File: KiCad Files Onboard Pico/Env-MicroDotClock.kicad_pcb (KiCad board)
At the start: 2 copper layers, 110 x 80 mm, 95 parts, among them IC1 IS31FL3730-QFLS2-TR, IC2 IS31FL3730-QFLS2-TR, IC3 IS31FL3730-QFLS2-TR, IC4 IS31FL3730-QFLS2-TR, J1 1mm 1x3, J2 GT-USB-7051A, J3 Button, J4 TYPE-C-31-M-12, M1 Dip-14 Socket, M2 Dip-14 Socket, M3 Dip-14 Socket, M4 Dip-14 Socket, M5 Dip-14 Socket, M6 Dip-14 Socket, M7 Dip-14 Socket, M8 Dip-14 Socket, Q1 2SC1815, SW1 MX Keyboard Switch, SW2 MX Keyboard Switch, SW3 MX Keyboard Switch, SW4 MX Keyboard Switch, SW5 MX Keyboard Switch, U1 TCA9406DC, U2 TPS63001DRCR, U3 DS3231M, U4 RP2040, Y1 3225_4P 12MHz

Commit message: removed sockets, added level shifter IC, changed RTC to smaller package, re-did entire board to be more tidy.
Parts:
- removed C23: 1uf 0402, Capacitor_SMD:C_0402_1005Metric
- removed C24, C26, C27, C28, C29, C30, C31: 100nf 0402, Capacitor_SMD:C_0402_1005Metric
- removed C25: 2.2uF 0402, Capacitor_SMD:C_0402_1005Metric
- removed C32: 10uF 0402, Capacitor_SMD:C_0402_1005Metric
- removed FLASH1: W25Q16JVUXIQ, Package_SON:SON-8-1EP_3x2mm_P0.5mm_EP1.4x1.6mm
- removed J2: GT-USB-7051A, Connector_USB:USB_C_Receptacle_G-Switch_GT-USB-7051x
- removed J3: Button, Button_Switch_SMD:SW_Push_SPST_NO_Alps_SKRK
- removed J4: TYPE-C-31-M-12, Connector_USB:USB_C_Receptacle_HRO_TYPE-C-31-M-12
- removed L1: SPH3015H2R2MT, Inductor_SMD:L_Sunlord_SWPA3015S
- removed M1, M2, M3, M4, M5, M6, M7, M8: Dip-14 Socket, Package_DIP:DIP-14_W7.62mm_Socket
- removed R14, R17: 5.1K 0805, Resistor_SMD:R_0805_2012Metric
- removed R15, R16: 5.1K 0402, Resistor_SMD:R_0402_1005Metric
- removed R18, R23: 1K 0402, Resistor_SMD:R_0402_1005Metric
- removed R19: 100ohm 0402, Resistor_SMD:R_0402_1005Metric
- removed R21: 10K 0402, Resistor_SMD:R_0402_1005Metric
- removed R24, R25: 27r 0402 resistor, Resistor_SMD:R_0402_1005Metric
- removed RSW1: TSA343G00-250J2, Button_Switch_SMD:SW_Push_SPST_NO_Alps_SKRK
- removed TP1, TP2, TP3: TestPoint, TestPoint:TestPoint_Pad_D1.0mm
- removed U2: TPS63001DRCR, Package_SON:Texas_DRC0010J_ThermalVias
- removed U4: RP2040, MCU_RaspberryPi_and_Boards:RP2040-QFN-56
- removed Y1: 3225_4P 12MHz, Crystal:Crystal_SMD_3225-4Pin_3.2x2.5mm
- added C201: 10uF 0402, Capacitor_SMD:C_0402_1005Metric, F.Cu at (81.7, 62.6)
- added C202: 0.1uF 0402, Capacitor_SMD:C_0402_1005Metric, F.Cu at (86.9, 60.6)
- added C203: 22pf 0402, Capacitor_SMD:C_0402_1005Metric, F.Cu at (62.5, 69.9)
- added C204: 22pf 0402, Capacitor_SMD:C_0402_1005Metric, F.Cu at (67.3, 72.5)
- added C205: 100nf 0402, Capacitor_SMD:C_0402_1005Metric, F.Cu at (66.2, 54.9)
- added C206: 10uF 0402, Capacitor_SMD:C_0402_1005Metric, F.Cu at (74.1, 56.2)
- added C207: 10uF 0402, Capacitor_SMD:C_0402_1005Metric, F.Cu at (75.0, 56.2)
- added C208: 100nf 0402, Capacitor_SMD:C_0402_1005Metric, F.Cu at (69.7, 69.5)
- added C209: 100nf 0402, Capacitor_SMD:C_0402_1005Metric, F.Cu at (67.5, 55.9)
- added C210: 1uf 0402, Capacitor_SMD:C_0402_1005Metric, F.Cu at (71.5, 55.9)
- added C211: 100nf 0402, Capacitor_SMD:C_0402_1005Metric, F.Cu at (73.6, 60.0)
- added C212: 2.2uF 0402, Capacitor_SMD:C_0402_1005Metric, F.Cu at (72.5, 55.9)
- added C213: 100nf 0402, Capacitor_SMD:C_0402_1005Metric, F.Cu at (74.6, 64.0)
- added C214: 100nf 0402, Capacitor_SMD:C_0402_1005Metric, F.Cu at (68.7, 69.5)
- added C215: 100nf 0402, Capacitor_SMD:C_0402_1005Metric, F.Cu at (62.3, 64.0)
- added C216: 100nf 0402, Capacitor_SMD:C_0402_1005Metric, F.Cu at (62.9, 59.7)
- added C217: 100nf 0402, Capacitor_SMD:C_0402_1005Metric, F.Cu at (68.5, 55.9)
- added C218: 100nf 0402, Capacitor_SMD:C_0402_1005Metric, F.Cu at (73.6, 59.0)
- added D10: LED 0402 10mA, LED_SMD:LED_0402_1005Metric, F.Cu at (35.5, 29.8)
- added D100: LED 0402 10mA, LED_SMD:LED_0402_1005Metric, F.Cu at (56.5, 37.8)
- added D101: LED 0402 10mA, LED_SMD:LED_0402_1005Metric, F.Cu at (56.5, 39.8)
- added D102: LED 0402 10mA, LED_SMD:LED_0402_1005Metric, F.Cu at (58.0, 27.8)
- added D103: LED 0402 10mA, LED_SMD:LED_0402_1005Metric, F.Cu at (58.0, 29.8)
- added D104: LED 0402 10mA, LED_SMD:LED_0402_1005Metric, F.Cu at (58.0, 31.8)
- added D105: LED 0402 10mA, LED_SMD:LED_0402_1005Metric, F.Cu at (58.0, 33.8)
- added D106: LED 0402 10mA, LED_SMD:LED_0402_1005Metric, F.Cu at (58.0, 35.8)
- added D107: LED 0402 10mA, LED_SMD:LED_0402_1005Metric, F.Cu at (58.0, 37.8)
- added D108: LED 0402 10mA, LED_SMD:LED_0402_1005Metric, F.Cu at (58.0, 39.8)
- added D109: LED 0402 10mA, LED_SMD:LED_0402_1005Metric, F.Cu at (59.5, 39.8)
- added D11: LED 0402 10mA, LED_SMD:LED_0402_1005Metric, F.Cu at (35.5, 31.8)
- added D110: LED 0402 10mA, LED_SMD:LED_0402_1005Metric, F.Cu at (61.0, 27.8)
- added D111: LED 0402 10mA, LED_SMD:LED_0402_1005Metric, F.Cu at (61.0, 29.8)
- added D112: LED 0402 10mA, LED_SMD:LED_0402_1005Metric, F.Cu at (61.0, 31.8)
- added D113: LED 0402 10mA, LED_SMD:LED_0402_1005Metric, F.Cu at (61.0, 33.8)
- added D114: LED 0402 10mA, LED_SMD:LED_0402_1005Metric, F.Cu at (61.0, 35.8)
- added D115: LED 0402 10mA, LED_SMD:LED_0402_1005Metric, F.Cu at (61.0, 37.8)
- added D116: LED 0402 10mA, LED_SMD:LED_0402_1005Metric, F.Cu at (61.0, 39.8)
- added D117: LED 0402 10mA, LED_SMD:LED_0402_1005Metric, F.Cu at (62.5, 27.8)
- added D118: LED 0402 10mA, LED_SMD:LED_0402_1005Metric, F.Cu at (62.5, 29.8)
- added D119: LED 0402 10mA, LED_SMD:LED_0402_1005Metric, F.Cu at (62.5, 31.8)
- added D12: LED 0402 10mA, LED_SMD:LED_0402_1005Metric, F.Cu at (35.5, 33.8)
- added D120: LED 0402 10mA, LED_SMD:LED_0402_1005Metric, F.Cu at (62.5, 33.8)
- added D121: LED 0402 10mA, LED_SMD:LED_0402_1005Metric, F.Cu at (62.5, 35.8)
- added D122: LED 0402 10mA, LED_SMD:LED_0402_1005Metric, F.Cu at (62.5, 37.8)
- added D123: LED 0402 10mA, LED_SMD:LED_0402_1005Metric, F.Cu at (62.5, 39.8)
- added D124: LED 0402 10mA, LED_SMD:LED_0402_1005Metric, F.Cu at (64.0, 27.8)
- added D125: LED 0402 10mA, LED_SMD:LED_0402_1005Metric, F.Cu at (64.0, 29.8)
- added D126: LED 0402 10mA, LED_SMD:LED_0402_1005Metric, F.Cu at (64.0, 31.8)
- added D127: LED 0402 10mA, LED_SMD:LED_0402_1005Metric, F.Cu at (64.0, 33.8)
- added D128: LED 0402 10mA, LED_SMD:LED_0402_1005Metric, F.Cu at (64.0, 35.8)
- added D129: LED 0402 10mA, LED_SMD:LED_0402_1005Metric, F.Cu at (64.0, 37.8)
- added D13: LED 0402 10mA, LED_SMD:LED_0402_1005Metric, F.Cu at (35.5, 35.8)
- added D130: LED 0402 10mA, LED_SMD:LED_0402_1005Metric, F.Cu at (64.0, 39.8)
- added D131: LED 0402 10mA, LED_SMD:LED_0402_1005Metric, F.Cu at (65.5, 27.8)
- added D132: LED 0402 10mA, LED_SMD:LED_0402_1005Metric, F.Cu at (65.5, 29.8)
- added D133: LED 0402 10mA, LED_SMD:LED_0402_1005Metric, F.Cu at (65.5, 31.8)
- added D134: LED 0402 10mA, LED_SMD:LED_0402_1005Metric, F.Cu at (65.5, 33.8)
- added D135: LED 0402 10mA, LED_SMD:LED_0402_1005Metric, F.Cu at (65.5, 35.8)
- added D136: LED 0402 10mA, LED_SMD:LED_0402_1005Metric, F.Cu at (65.5, 37.8)
- added D137: LED 0402 10mA, LED_SMD:LED_0402_1005Metric, F.Cu at (65.5, 39.8)
- added D138: LED 0402 10mA, LED_SMD:LED_0402_1005Metric, F.Cu at (67.0, 27.8)
- added D139: LED 0402 10mA, LED_SMD:LED_0402_1005Metric, F.Cu at (67.0, 29.8)
- added D14: LED 0402 10mA, LED_SMD:LED_0402_1005Metric, F.Cu at (35.5, 37.8)
- added D140: LED 0402 10mA, LED_SMD:LED_0402_1005Metric, F.Cu at (67.0, 31.8)
- added D141: LED 0402 10mA, LED_SMD:LED_0402_1005Metric, F.Cu at (67.0, 33.8)
- added D142: LED 0402 10mA, LED_SMD:LED_0402_1005Metric, F.Cu at (67.0, 35.8)
- added D143: LED 0402 10mA, LED_SMD:LED_0402_1005Metric, F.Cu at (67.0, 37.8)
- added D144: LED 0402 10mA, LED_SMD:LED_0402_1005Metric, F.Cu at (67.0, 39.8)
- added D145: LED 0402 10mA, LED_SMD:LED_0402_1005Metric, F.Cu at (68.5, 39.8)
- added D146: LED 0402 10mA, LED_SMD:LED_0402_1005Metric, F.Cu at (70.0, 27.8)
- added D147: LED 0402 10mA, LED_SMD:LED_0402_1005Metric, F.Cu at (70.0, 29.8)
- added D148: LED 0402 10mA, LED_SMD:LED_0402_1005Metric, F.Cu at (70.0, 31.8)
- added D149: LED 0402 10mA, LED_SMD:LED_0402_1005Metric, F.Cu at (70.0, 33.8)
- added D15: LED 0402 10mA, LED_SMD:LED_0402_1005Metric, F.Cu at (35.5, 39.8)
- added D150: LED 0402 10mA, LED_SMD:LED_0402_1005Metric, F.Cu at (70.0, 35.8)
- added D151: LED 0402 10mA, LED_SMD:LED_0402_1005Metric, F.Cu at (70.0, 37.8)
- added D152: LED 0402 10mA, LED_SMD:LED_0402_1005Metric, F.Cu at (70.0, 39.8)
- added D153: LED 0402 10mA, LED_SMD:LED_0402_1005Metric, F.Cu at (71.5, 27.8)
- added D154: LED 0402 10mA, LED_SMD:LED_0402_1005Metric, F.Cu at (71.5, 29.8)
- added D155: LED 0402 10mA, LED_SMD:LED_0402_1005Metric, F.Cu at (71.5, 31.8)
- added D156: LED 0402 10mA, LED_SMD:LED_0402_1005Metric, F.Cu at (71.5, 33.8)
- added D157: LED 0402 10mA, LED_SMD:LED_0402_1005Metric, F.Cu at (71.5, 35.8)
- added D158: LED 0402 10mA, LED_SMD:LED_0402_1005Metric, F.Cu at (71.5, 37.8)
- added D159: LED 0402 10mA, LED_SMD:LED_0402_1005Metric, F.Cu at (71.5, 39.8)
- added D16: LED 0402 10mA, LED_SMD:LED_0402_1005Metric, F.Cu at (37.0, 27.8)
- added D160: LED 0402 10mA, LED_SMD:LED_0402_1005Metric, F.Cu at (73.0, 27.8)
- added D161: LED 0402 10mA, LED_SMD:LED_0402_1005Metric, F.Cu at (73.0, 29.8)
- added D162: LED 0402 10mA, LED_SMD:LED_0402_1005Metric, F.Cu at (73.0, 31.8)
- added D163: LED 0402 10mA, LED_SMD:LED_0402_1005Metric, F.Cu at (73.0, 33.8)
- added D164: LED 0402 10mA, LED_SMD:LED_0402_1005Metric, F.Cu at (73.0, 35.8)
- added D165: LED 0402 10mA, LED_SMD:LED_0402_1005Metric, F.Cu at (73.0, 37.8)
- added D166: LED 0402 10mA, LED_SMD:LED_0402_1005Metric, F.Cu at (73.0, 39.8)
- added D167: LED 0402 10mA, LED_SMD:LED_0402_1005Metric, F.Cu at (74.5, 27.8)
- added D168: LED 0402 10mA, LED_SMD:LED_0402_1005Metric, F.Cu at (74.5, 29.8)
- added D169: LED 0402 10mA, LED_SMD:LED_0402_1005Metric, F.Cu at (74.5, 31.8)
- added D17: LED 0402 10mA, LED_SMD:LED_0402_1005Metric, F.Cu at (37.0, 29.8)
- added D170: LED 0402 10mA, LED_SMD:LED_0402_1005Metric, F.Cu at (74.5, 33.8)
- added D171: LED 0402 10mA, LED_SMD:LED_0402_1005Metric, F.Cu at (74.5, 35.8)
- added D172: LED 0402 10mA, LED_SMD:LED_0402_1005Metric, F.Cu at (74.5, 37.8)
- added D173: LED 0402 10mA, LED_SMD:LED_0402_1005Metric, F.Cu at (74.5, 39.8)
- added D174: LED 0402 10mA, LED_SMD:LED_0402_1005Metric, F.Cu at (76.0, 27.8)
- added D175: LED 0402 10mA, LED_SMD:LED_0402_1005Metric, F.Cu at (76.0, 29.8)
- added D176: LED 0402 10mA, LED_SMD:LED_0402_1005Metric, F.Cu at (76.0, 31.8)
- added D177: LED 0402 10mA, LED_SMD:LED_0402_1005Metric, F.Cu at (76.0, 33.8)
- added D178: LED 0402 10mA, LED_SMD:LED_0402_1005Metric, F.Cu at (76.0, 35.8)
- added D179: LED 0402 10mA, LED_SMD:LED_0402_1005Metric, F.Cu at (76.0, 37.8)
- added D18: LED 0402 10mA, LED_SMD:LED_0402_1005Metric, F.Cu at (37.0, 31.8)
- added D180: LED 0402 10mA, LED_SMD:LED_0402_1005Metric, F.Cu at (76.0, 39.8)
- added D181: LED 0402 10mA, LED_SMD:LED_0402_1005Metric, F.Cu at (77.5, 39.8)
- added D182: LED 0402 10mA, LED_SMD:LED_0402_1005Metric, F.Cu at (79.0, 27.8)
- added D183: LED 0402 10mA, LED_SMD:LED_0402_1005Metric, F.Cu at (79.0, 29.8)
- added D184: LED 0402 10mA, LED_SMD:LED_0402_1005Metric, F.Cu at (79.0, 31.8)
- added D185: LED 0402 10mA, LED_SMD:LED_0402_1005Metric, F.Cu at (79.0, 33.8)
- added D186: LED 0402 10mA, LED_SMD:LED_0402_1005Metric, F.Cu at (79.0, 35.8)
- added D187: LED 0402 10mA, LED_SMD:LED_0402_1005Metric, F.Cu at (79.0, 37.8)
- added D188: LED 0402 10mA, LED_SMD:LED_0402_1005Metric, F.Cu at (79.0, 39.8)
- added D189: LED 0402 10mA, LED_SMD:LED_0402_1005Metric, F.Cu at (80.5, 27.8)
- added D19: LED 0402 10mA, LED_SMD:LED_0402_1005Metric, F.Cu at (37.0, 33.8)
- added D190: LED 0402 10mA, LED_SMD:LED_0402_1005Metric, F.Cu at (80.5, 29.8)
- added D191: LED 0402 10mA, LED_SMD:LED_0402_1005Metric, F.Cu at (80.5, 31.8)
- added D192: LED 0402 10mA, LED_SMD:LED_0402_1005Metric, F.Cu at (80.5, 33.8)
- added D193: LED 0402 10mA, LED_SMD:LED_0402_1005Metric, F.Cu at (80.5, 35.8)
- added D194: LED 0402 10mA, LED_SMD:LED_0402_1005Metric, F.Cu at (80.5, 37.8)
- added D195: LED 0402 10mA, LED_SMD:LED_0402_1005Metric, F.Cu at (80.5, 39.8)
- added D196: LED 0402 10mA, LED_SMD:LED_0402_1005Metric, F.Cu at (82.0, 27.8)
- added D197: LED 0402 10mA, LED_SMD:LED_0402_1005Metric, F.Cu at (82.0, 29.8)
- added D198: LED 0402 10mA, LED_SMD:LED_0402_1005Metric, F.Cu at (82.0, 31.8)
- added D199: LED 0402 10mA, LED_SMD:LED_0402_1005Metric, F.Cu at (82.0, 33.8)
- added D20: LED 0402 10mA, LED_SMD:LED_0402_1005Metric, F.Cu at (37.0, 35.8)
- added D200: LED 0402 10mA, LED_SMD:LED_0402_1005Metric, F.Cu at (82.0, 35.8)
- added D201: LED 0402 10mA, LED_SMD:LED_0402_1005Metric, F.Cu at (82.0, 37.8)
- added D202: LED 0402 10mA, LED_SMD:LED_0402_1005Metric, F.Cu at (82.0, 39.8)
- added D203: LED 0402 10mA, LED_SMD:LED_0402_1005Metric, F.Cu at (83.5, 27.8)
- added D204: LED 0402 10mA, LED_SMD:LED_0402_1005Metric, F.Cu at (83.5, 29.8)
- added D205: LED 0402 10mA, LED_SMD:LED_0402_1005Metric, F.Cu at (83.5, 31.8)
- added D206: LED 0402 10mA, LED_SMD:LED_0402_1005Metric, F.Cu at (83.5, 33.8)
- added D207: LED 0402 10mA, LED_SMD:LED_0402_1005Metric, F.Cu at (83.5, 35.8)
- added D208: LED 0402 10mA, LED_SMD:LED_0402_1005Metric, F.Cu at (83.5, 37.8)
- added D209: LED 0402 10mA, LED_SMD:LED_0402_1005Metric, F.Cu at (83.5, 39.8)
- added D21: LED 0402 10mA, LED_SMD:LED_0402_1005Metric, F.Cu at (37.0, 37.8)
- added D210: LED 0402 10mA, LED_SMD:LED_0402_1005Metric, F.Cu at (85.0, 27.8)
- added D211: LED 0402 10mA, LED_SMD:LED_0402_1005Metric, F.Cu at (85.0, 29.8)
- added D212: LED 0402 10mA, LED_SMD:LED_0402_1005Metric, F.Cu at (85.0, 31.8)
- added D213: LED 0402 10mA, LED_SMD:LED_0402_1005Metric, F.Cu at (85.0, 33.8)
- added D214: LED 0402 10mA, LED_SMD:LED_0402_1005Metric, F.Cu at (85.0, 35.8)
- added D215: LED 0402 10mA, LED_SMD:LED_0402_1005Metric, F.Cu at (85.0, 37.8)
- added D216: LED 0402 10mA, LED_SMD:LED_0402_1005Metric, F.Cu at (85.0, 39.8)
- added D217: LED 0402 10mA, LED_SMD:LED_0402_1005Metric, F.Cu at (86.5, 39.8)
- added D218: LED 0402 10mA, LED_SMD:LED_0402_1005Metric, F.Cu at (88.0, 27.8)
- added D219: LED 0402 10mA, LED_SMD:LED_0402_1005Metric, F.Cu at (88.0, 29.8)
- added D22: LED 0402 10mA, LED_SMD:LED_0402_1005Metric, F.Cu at (37.0, 39.8)
- added D220: LED 0402 10mA, LED_SMD:LED_0402_1005Metric, F.Cu at (88.0, 31.8)
- added D221: LED 0402 10mA, LED_SMD:LED_0402_1005Metric, F.Cu at (88.0, 33.8)
- added D222: LED 0402 10mA, LED_SMD:LED_0402_1005Metric, F.Cu at (88.0, 35.8)
- added D223: LED 0402 10mA, LED_SMD:LED_0402_1005Metric, F.Cu at (88.0, 37.8)
- added D224: LED 0402 10mA, LED_SMD:LED_0402_1005Metric, F.Cu at (88.0, 39.8)
- added D225: LED 0402 10mA, LED_SMD:LED_0402_1005Metric, F.Cu at (89.5, 27.8)
- added D226: LED 0402 10mA, LED_SMD:LED_0402_1005Metric, F.Cu at (89.5, 29.8)
- added D227: LED 0402 10mA, LED_SMD:LED_0402_1005Metric, F.Cu at (89.5, 31.8)
- added D228: LED 0402 10mA, LED_SMD:LED_0402_1005Metric, F.Cu at (89.5, 33.8)
- added D229: LED 0402 10mA, LED_SMD:LED_0402_1005Metric, F.Cu at (89.5, 35.8)
- added D23: LED 0402 10mA, LED_SMD:LED_0402_1005Metric, F.Cu at (38.5, 27.8)
- added D230: LED 0402 10mA, LED_SMD:LED_0402_1005Metric, F.Cu at (89.5, 37.8)
- added D231: LED 0402 10mA, LED_SMD:LED_0402_1005Metric, F.Cu at (89.5, 39.8)
- added D232: LED 0402 10mA, LED_SMD:LED_0402_1005Metric, F.Cu at (91.0, 27.8)
- added D233: LED 0402 10mA, LED_SMD:LED_0402_1005Metric, F.Cu at (91.0, 29.8)
- added D234: LED 0402 10mA, LED_SMD:LED_0402_1005Metric, F.Cu at (91.0, 31.8)
- added D235: LED 0402 10mA, LED_SMD:LED_0402_1005Metric, F.Cu at (91.0, 33.8)
- added D236: LED 0402 10mA, LED_SMD:LED_0402_1005Metric, F.Cu at (91.0, 35.8)
- added D237: LED 0402 10mA, LED_SMD:LED_0402_1005Metric, F.Cu at (91.0, 37.8)
- added D238: LED 0402 10mA, LED_SMD:LED_0402_1005Metric, F.Cu at (91.0, 39.8)
- added D239: LED 0402 10mA, LED_SMD:LED_0402_1005Metric, F.Cu at (92.5, 27.8)
- added D24: LED 0402 10mA, LED_SMD:LED_0402_1005Metric, F.Cu at (38.5, 29.8)
- added D240: LED 0402 10mA, LED_SMD:LED_0402_1005Metric, F.Cu at (92.5, 29.8)
- added D241: LED 0402 10mA, LED_SMD:LED_0402_1005Metric, F.Cu at (92.5, 31.8)
- added D242: LED 0402 10mA, LED_SMD:LED_0402_1005Metric, F.Cu at (92.5, 33.8)
- added D243: LED 0402 10mA, LED_SMD:LED_0402_1005Metric, F.Cu at (92.5, 35.8)
- added D244: LED 0402 10mA, LED_SMD:LED_0402_1005Metric, F.Cu at (92.5, 37.8)
- added D245: LED 0402 10mA, LED_SMD:LED_0402_1005Metric, F.Cu at (92.5, 39.8)
- added D246: LED 0402 10mA, LED_SMD:LED_0402_1005Metric, F.Cu at (94.0, 27.8)
- added D247: LED 0402 10mA, LED_SMD:LED_0402_1005Metric, F.Cu at (94.0, 29.8)
- added D248: LED 0402 10mA, LED_SMD:LED_0402_1005Metric, F.Cu at (94.0, 31.8)
- added D249: LED 0402 10mA, LED_SMD:LED_0402_1005Metric, F.Cu at (94.0, 33.8)
- added D25: LED 0402 10mA, LED_SMD:LED_0402_1005Metric, F.Cu at (38.5, 31.8)
- added D250: LED 0402 10mA, LED_SMD:LED_0402_1005Metric, F.Cu at (94.0, 35.8)
- added D251: LED 0402 10mA, LED_SMD:LED_0402_1005Metric, F.Cu at (94.0, 37.8)
- added D252: LED 0402 10mA, LED_SMD:LED_0402_1005Metric, F.Cu at (94.0, 39.8)
- added D253: LED 0402 10mA, LED_SMD:LED_0402_1005Metric, F.Cu at (95.5, 39.8)
- added D254: LED 0402 10mA, LED_SMD:LED_0402_1005Metric, F.Cu at (97.0, 27.8)
- added D255: LED 0402 10mA, LED_SMD:LED_0402_1005Metric, F.Cu at (97.0, 29.8)
- added D256: LED 0402 10mA, LED_SMD:LED_0402_1005Metric, F.Cu at (97.0, 31.8)
- added D257: LED 0402 10mA, LED_SMD:LED_0402_1005Metric, F.Cu at (97.0, 33.8)
- added D258: LED 0402 10mA, LED_SMD:LED_0402_1005Metric, F.Cu at (97.0, 35.8)
- added D259: LED 0402 10mA, LED_SMD:LED_0402_1005Metric, F.Cu at (97.0, 37.8)
- added D26: LED 0402 10mA, LED_SMD:LED_0402_1005Metric, F.Cu at (38.5, 33.8)
- added D260: LED 0402 10mA, LED_SMD:LED_0402_1005Metric, F.Cu at (97.0, 39.8)
- added D261: LED 0402 10mA, LED_SMD:LED_0402_1005Metric, F.Cu at (98.5, 27.8)
- added D262: LED 0402 10mA, LED_SMD:LED_0402_1005Metric, F.Cu at (98.5, 29.8)
- added D263: LED 0402 10mA, LED_SMD:LED_0402_1005Metric, F.Cu at (98.5, 31.8)
- added D264: LED 0402 10mA, LED_SMD:LED_0402_1005Metric, F.Cu at (98.5, 33.8)
- added D265: LED 0402 10mA, LED_SMD:LED_0402_1005Metric, F.Cu at (98.5, 35.8)
- added D266: LED 0402 10mA, LED_SMD:LED_0402_1005Metric, F.Cu at (98.5, 37.8)
- added D267: LED 0402 10mA, LED_SMD:LED_0402_1005Metric, F.Cu at (98.5, 39.8)
- added D268: LED 0402 10mA, LED_SMD:LED_0402_1005Metric, F.Cu at (100.0, 27.8)
- added D269: LED 0402 10mA, LED_SMD:LED_0402_1005Metric, F.Cu at (100.0, 29.8)
- added D27: LED 0402 10mA, LED_SMD:LED_0402_1005Metric, F.Cu at (38.5, 35.8)
- added D270: LED 0402 10mA, LED_SMD:LED_0402_1005Metric, F.Cu at (100.0, 31.8)
- added D271: LED 0402 10mA, LED_SMD:LED_0402_1005Metric, F.Cu at (100.0, 33.8)
- added D272: LED 0402 10mA, LED_SMD:LED_0402_1005Metric, F.Cu at (100.0, 35.8)
- added D273: LED 0402 10mA, LED_SMD:LED_0402_1005Metric, F.Cu at (100.0, 37.8)
- added D274: LED 0402 10mA, LED_SMD:LED_0402_1005Metric, F.Cu at (100.0, 39.8)
- added D275: LED 0402 10mA, LED_SMD:LED_0402_1005Metric, F.Cu at (101.5, 27.8)
- added D276: LED 0402 10mA, LED_SMD:LED_0402_1005Metric, F.Cu at (101.5, 29.8)
- added D277: LED 0402 10mA, LED_SMD:LED_0402_1005Metric, F.Cu at (101.5, 31.8)
- added D278: LED 0402 10mA, LED_SMD:LED_0402_1005Metric, F.Cu at (101.5, 33.8)
- added D279: LED 0402 10mA, LED_SMD:LED_0402_1005Metric, F.Cu at (101.5, 35.8)
- added D28: LED 0402 10mA, LED_SMD:LED_0402_1005Metric, F.Cu at (38.5, 37.8)
- added D280: LED 0402 10mA, LED_SMD:LED_0402_1005Metric, F.Cu at (101.5, 37.8)
- added D281: LED 0402 10mA, LED_SMD:LED_0402_1005Metric, F.Cu at (101.5, 39.8)
- added D282: LED 0402 10mA, LED_SMD:LED_0402_1005Metric, F.Cu at (103.0, 27.8)
- added D283: LED 0402 10mA, LED_SMD:LED_0402_1005Metric, F.Cu at (103.0, 29.8)
- added D284: LED 0402 10mA, LED_SMD:LED_0402_1005Metric, F.Cu at (103.0, 31.8)
- added D285: LED 0402 10mA, LED_SMD:LED_0402_1005Metric, F.Cu at (103.0, 33.8)
- added D286: LED 0402 10mA, LED_SMD:LED_0402_1005Metric, F.Cu at (103.0, 35.8)
- added D287: LED 0402 10mA, LED_SMD:LED_0402_1005Metric, F.Cu at (103.0, 37.8)
- added D288: LED 0402 10mA, LED_SMD:LED_0402_1005Metric, F.Cu at (103.0, 39.8)
- added D29: LED 0402 10mA, LED_SMD:LED_0402_1005Metric, F.Cu at (38.5, 39.8)
- added D3: LED 0402 10mA, LED_SMD:LED_0402_1005Metric, F.Cu at (34.0, 29.8)
- added D30: LED 0402 10mA, LED_SMD:LED_0402_1005Metric, F.Cu at (40.0, 27.8)
- added D31: LED 0402 10mA, LED_SMD:LED_0402_1005Metric, F.Cu at (40.0, 29.8)
- added D32: LED 0402 10mA, LED_SMD:LED_0402_1005Metric, F.Cu at (40.0, 31.8)
- added D33: LED 0402 10mA, LED_SMD:LED_0402_1005Metric, F.Cu at (40.0, 33.8)
- added D34: LED 0402 10mA, LED_SMD:LED_0402_1005Metric, F.Cu at (40.0, 35.8)
- added D35: LED 0402 10mA, LED_SMD:LED_0402_1005Metric, F.Cu at (40.0, 37.8)
- added D36: LED 0402 10mA, LED_SMD:LED_0402_1005Metric, F.Cu at (40.0, 39.8)
- added D37: LED 0402 10mA, LED_SMD:LED_0402_1005Metric, F.Cu at (41.5, 39.8)
- added D38: LED 0402 10mA, LED_SMD:LED_0402_1005Metric, F.Cu at (43.0, 27.8)
- added D39: LED 0402 10mA, LED_SMD:LED_0402_1005Metric, F.Cu at (43.0, 29.8)
- added D4: LED 0402 10mA, LED_SMD:LED_0402_1005Metric, F.Cu at (34.0, 31.8)
- added D40: LED 0402 10mA, LED_SMD:LED_0402_1005Metric, F.Cu at (43.0, 31.8)
- added D41: LED 0402 10mA, LED_SMD:LED_0402_1005Metric, F.Cu at (43.0, 33.8)
- added D42: LED 0402 10mA, LED_SMD:LED_0402_1005Metric, F.Cu at (43.0, 35.8)
- added D43: LED 0402 10mA, LED_SMD:LED_0402_1005Metric, F.Cu at (43.0, 37.8)
- added D44: LED 0402 10mA, LED_SMD:LED_0402_1005Metric, F.Cu at (43.0, 39.8)
- added D45: LED 0402 10mA, LED_SMD:LED_0402_1005Metric, F.Cu at (44.5, 27.8)
- added D46: LED 0402 10mA, LED_SMD:LED_0402_1005Metric, F.Cu at (44.5, 29.8)
- added D47: LED 0402 10mA, LED_SMD:LED_0402_1005Metric, F.Cu at (44.5, 31.8)
- added D48: LED 0402 10mA, LED_SMD:LED_0402_1005Metric, F.Cu at (44.5, 33.8)
- added D49: LED 0402 10mA, LED_SMD:LED_0402_1005Metric, F.Cu at (44.5, 35.8)
- added D5: LED 0402 10mA, LED_SMD:LED_0402_1005Metric, F.Cu at (34.0, 33.8)
- added D50: LED 0402 10mA, LED_SMD:LED_0402_1005Metric, F.Cu at (44.5, 37.8)
- added D51: LED 0402 10mA, LED_SMD:LED_0402_1005Metric, F.Cu at (44.5, 39.8)
- added D52: LED 0402 10mA, LED_SMD:LED_0402_1005Metric, F.Cu at (46.0, 27.8)
- added D53: LED 0402 10mA, LED_SMD:LED_0402_1005Metric, F.Cu at (46.0, 29.8)
- added D54: LED 0402 10mA, LED_SMD:LED_0402_1005Metric, F.Cu at (46.0, 31.8)
- added D55: LED 0402 10mA, LED_SMD:LED_0402_1005Metric, F.Cu at (46.0, 33.8)
- added D56: LED 0402 10mA, LED_SMD:LED_0402_1005Metric, F.Cu at (46.0, 35.8)
- added D57: LED 0402 10mA, LED_SMD:LED_0402_1005Metric, F.Cu at (46.0, 37.8)
- added D58: LED 0402 10mA, LED_SMD:LED_0402_1005Metric, F.Cu at (46.0, 39.8)
- added D59: LED 0402 10mA, LED_SMD:LED_0402_1005Metric, F.Cu at (47.5, 27.8)
- added D6: LED 0402 10mA, LED_SMD:LED_0402_1005Metric, F.Cu at (34.0, 35.8)
- added D60: LED 0402 10mA, LED_SMD:LED_0402_1005Metric, F.Cu at (47.5, 29.8)
- added D61: LED 0402 10mA, LED_SMD:LED_0402_1005Metric, F.Cu at (47.5, 31.8)
- added D62: LED 0402 10mA, LED_SMD:LED_0402_1005Metric, F.Cu at (47.5, 33.8)
- added D63: LED 0402 10mA, LED_SMD:LED_0402_1005Metric, F.Cu at (47.5, 35.8)
- added D64: LED 0402 10mA, LED_SMD:LED_0402_1005Metric, F.Cu at (47.5, 37.8)
- added D65: LED 0402 10mA, LED_SMD:LED_0402_1005Metric, F.Cu at (47.5, 39.8)
- added D66: LED 0402 10mA, LED_SMD:LED_0402_1005Metric, F.Cu at (49.0, 27.8)
- added D67: LED 0402 10mA, LED_SMD:LED_0402_1005Metric, F.Cu at (49.0, 29.8)
- added D68: LED 0402 10mA, LED_SMD:LED_0402_1005Metric, F.Cu at (49.0, 31.8)
- added D69: LED 0402 10mA, LED_SMD:LED_0402_1005Metric, F.Cu at (49.0, 33.8)
- added D7: LED 0402 10mA, LED_SMD:LED_0402_1005Metric, F.Cu at (34.0, 37.8)
- added D70: LED 0402 10mA, LED_SMD:LED_0402_1005Metric, F.Cu at (49.0, 35.8)
- added D71: LED 0402 10mA, LED_SMD:LED_0402_1005Metric, F.Cu at (49.0, 37.8)
- added D72: LED 0402 10mA, LED_SMD:LED_0402_1005Metric, F.Cu at (49.0, 39.8)
- added D73: LED 0402 10mA, LED_SMD:LED_0402_1005Metric, F.Cu at (50.5, 39.8)
- added D74: LED 0402 10mA, LED_SMD:LED_0402_1005Metric, F.Cu at (52.0, 27.8)
- added D75: LED 0402 10mA, LED_SMD:LED_0402_1005Metric, F.Cu at (52.0, 29.8)
- added D76: LED 0402 10mA, LED_SMD:LED_0402_1005Metric, F.Cu at (52.0, 31.8)
- added D77: LED 0402 10mA, LED_SMD:LED_0402_1005Metric, F.Cu at (52.0, 33.8)
- added D78: LED 0402 10mA, LED_SMD:LED_0402_1005Metric, F.Cu at (52.0, 35.8)
- added D79: LED 0402 10mA, LED_SMD:LED_0402_1005Metric, F.Cu at (52.0, 37.8)
- added D8: LED 0402 10mA, LED_SMD:LED_0402_1005Metric, F.Cu at (34.0, 39.8)
- added D80: LED 0402 10mA, LED_SMD:LED_0402_1005Metric, F.Cu at (52.0, 39.8)
- added D81: LED 0402 10mA, LED_SMD:LED_0402_1005Metric, F.Cu at (53.5, 27.8)
- added D82: LED 0402 10mA, LED_SMD:LED_0402_1005Metric, F.Cu at (53.5, 29.8)
- added D83: LED 0402 10mA, LED_SMD:LED_0402_1005Metric, F.Cu at (53.5, 31.8)
- added D84: LED 0402 10mA, LED_SMD:LED_0402_1005Metric, F.Cu at (53.5, 33.8)
- added D85: LED 0402 10mA, LED_SMD:LED_0402_1005Metric, F.Cu at (53.5, 35.8)
- added D86: LED 0402 10mA, LED_SMD:LED_0402_1005Metric, F.Cu at (53.5, 37.8)
- added D87: LED 0402 10mA, LED_SMD:LED_0402_1005Metric, F.Cu at (53.5, 39.8)
- added D88: LED 0402 10mA, LED_SMD:LED_0402_1005Metric, F.Cu at (55.0, 27.8)
- added D89: LED 0402 10mA, LED_SMD:LED_0402_1005Metric, F.Cu at (55.0, 29.8)
- added D9: LED 0402 10mA, LED_SMD:LED_0402_1005Metric, F.Cu at (35.5, 27.8)
- added D90: LED 0402 10mA, LED_SMD:LED_0402_1005Metric, F.Cu at (55.0, 31.8)
- added D91: LED 0402 10mA, LED_SMD:LED_0402_1005Metric, F.Cu at (55.0, 33.8)
- added D92: LED 0402 10mA, LED_SMD:LED_0402_1005Metric, F.Cu at (55.0, 35.8)
- added D93: LED 0402 10mA, LED_SMD:LED_0402_1005Metric, F.Cu at (55.0, 37.8)
- added D94: LED 0402 10mA, LED_SMD:LED_0402_1005Metric, F.Cu at (55.0, 39.8)
- added D95: LED 0402 10mA, LED_SMD:LED_0402_1005Metric, F.Cu at (56.5, 27.8)
- added D96: LED 0402 10mA, LED_SMD:LED_0402_1005Metric, F.Cu at (56.5, 29.8)
- added D97: LED 0402 10mA, LED_SMD:LED_0402_1005Metric, F.Cu at (56.5, 31.8)
- added D98: LED 0402 10mA, LED_SMD:LED_0402_1005Metric, F.Cu at (56.5, 33.8)
- added D99: LED 0402 10mA, LED_SMD:LED_0402_1005Metric, F.Cu at (56.5, 35.8)
- added DI201: 1N5819W, Diode_SMD:D_SOD-123, B.Cu at (88.5, 68.6)
- added FLASH201: W25Q16JVUXIQ, Package_SON:SON-8-1EP_3x2mm_P0.5mm_EP1.4x1.6mm, F.Cu at (64.8, 57.1)
- added J201: GT-USB-7051A, Connector_USB:USB_C_Receptacle_G-Switch_GT-USB-7051x, B.Cu at (91.3, 63.0)
- added J203: Button, Button_Switch_SMD:SW_SPST_B3U-1000P-B, F.Cu at (65.3, 51.4)
- added L201: SPH3015H2R2MT, Inductor_SMD:L_Sunlord_SWPA3015S, F.Cu at (79.9, 60.1)
- added R201: 5.1K 0402, Resistor_SMD:R_0402_1005Metric, B.Cu at (92.5, 58.8)
- added R202: 5.1K 0402, Resistor_SMD:R_0402_1005Metric, B.Cu at (90.2, 67.2)
- added R205: 100ohm 0402, Resistor_SMD:R_0402_1005Metric, F.Cu at (84.4, 62.6)
- added R206: 1K 0402, Resistor_SMD:R_0402_1005Metric, F.Cu at (64.8, 54.3)
- added R207: 10K 0402, Resistor_SMD:R_0402_1005Metric, F.Cu at (64.8, 55.3)
- added R208: 1K 0402, Resistor_SMD:R_0402_1005Metric, F.Cu at (67.3, 70.4)
- added R209: 27r 0402 resistor, Resistor_SMD:R_0402_1005Metric, F.Cu at (69.5, 55.9)
- added R210: 27r 0402 resistor, Resistor_SMD:R_0402_1005Metric, F.Cu at (70.5, 55.9)
- added RSW201: Button, Button_Switch_SMD:SW_SPST_B3U-1000P-B, F.Cu at (72.0, 69.5)
- added TP201: TestPoint, TestPoint:TestPoint_Pad_D1.0mm, F.Cu at (89.7, 58.4)
- added TP202: TestPoint, TestPoint:TestPoint_Pad_D1.0mm, F.Cu at (87.4, 58.4)
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- renumbered BT1 to BT2
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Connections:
- C1 pad 1: VCC -> GND
- C1 pad 2: GND -> Net-(IC1-C_FILT)
- C13 pad 1: VCC -> GND
- C13 pad 2: GND -> Net-(IC3-C_FILT)
- C14 pad 1: VCC -> GND
- C14 pad 2: GND -> Net-(IC3-IN)
- C15 pad 1: VSYS -> VCC
- C16 pad 1: GND -> VCC
- C16 pad 2: XIN -> GND
- C17 pad 1: GND -> VCC
- C17 pad 2: Net-(C17-Pad2) -> GND
- C18 pad 1: +3V3 -> GND
- C18 pad 2: GND -> Net-(IC4-C_FILT)
- C19 pad 1: Net-(U2-EN) -> GND
- C19 pad 2: GND -> Net-(IC4-IN)
- C2 pad 1: VCC -> GND
- C2 pad 2: GND -> Net-(IC1-IN)
- C20 pad 1: +3V3 -> VCC
- C21 pad 1: +1V1 -> VCC
- C22 pad 1: +1V1 -> VCC
- C6 pad 1: VCC -> GND
- C6 pad 2: GND -> Net-(IC2-C_FILT)
- C7 pad 1: VCC -> GND
- C7 pad 2: GND -> Net-(IC2-IN)
- D1 pad 1: VSYS -> IC1R7
- D1 pad 2: Net-(D1-A) -> IC1C8
- D2 pad 1: VSYS -> IC1R1
- D2 pad 2: Net-(D2-A) -> IC1C1
- IC1 pad 1: i2c-sda -> I2C_SDA_5V0
- IC1 pad 2: i2c-scl -> I2C_SCL_5V0
- IC1 pad 4: unconnected-(IC1-IN-Pad4) -> Net-(IC1-IN)
- IC1 pad 5: unconnected-(IC1-C_FILT-Pad5) -> Net-(IC1-C_FILT)
- IC2 pad 1: i2c-sda -> I2C_SDA_5V0
- IC2 pad 2: i2c-scl -> I2C_SCL_5V0
- IC2 pad 4: unconnected-(IC2-IN-Pad4) -> Net-(IC2-IN)
- IC2 pad 5: unconnected-(IC2-C_FILT-Pad5) -> Net-(IC2-C_FILT)
- IC3 pad 1: i2c-sda -> I2C_SDA_5V0
- IC3 pad 2: i2c-scl -> I2C_SCL_5V0
- IC3 pad 4: unconnected-(IC3-IN-Pad4) -> Net-(IC3-IN)
- IC3 pad 5: unconnected-(IC3-C_FILT-Pad5) -> Net-(IC3-C_FILT)
- IC3 pad 6: i2c-sda -> I2C_SDA_5V0
- IC4 pad 1: i2c-sda -> I2C_SDA_5V0
- IC4 pad 2: i2c-scl -> I2C_SCL_5V0
- IC4 pad 4: unconnected-(IC4-IN-Pad4) -> Net-(IC4-IN)
- IC4 pad 5: unconnected-(IC4-C_FILT-Pad5) -> Net-(IC4-C_FILT)
- IC4 pad 6: i2c-scl -> I2C_SCL_5V0
- R6 pad 1: i2c-scl -> I2C_SCL_5V0
- R7 pad 1: i2c-sda -> I2C_SDA_5V0
- U1 pad 1: i2c-sda -> I2C_SDA_5V0
- U1 pad 8: i2c-scl -> I2C_SCL_5V0
- U3 pad 2: VCC -> Net-(BT1-+)
- U3 pad 6: GND -> VCC
- U3 pad 7: GND -> I2C_SDA_5V0
- U3 pad 8: GND -> I2C_SCL_5V0
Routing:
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- added copper zone on F.Cu, net Net-(U201-L1)
- added copper zone on F.Cu, net Net-(U201-L2)
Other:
- board size 110 x 80 mm -> 94 x 80 mm
- board text removed: "BOOTSEL"
- board text removed: "D+/D-"
- board text removed: "PWR ONLY"
- board text removed: "RESET"
- board text removed: "SWD GND SWC"
- board text removed: "USB+DATA"

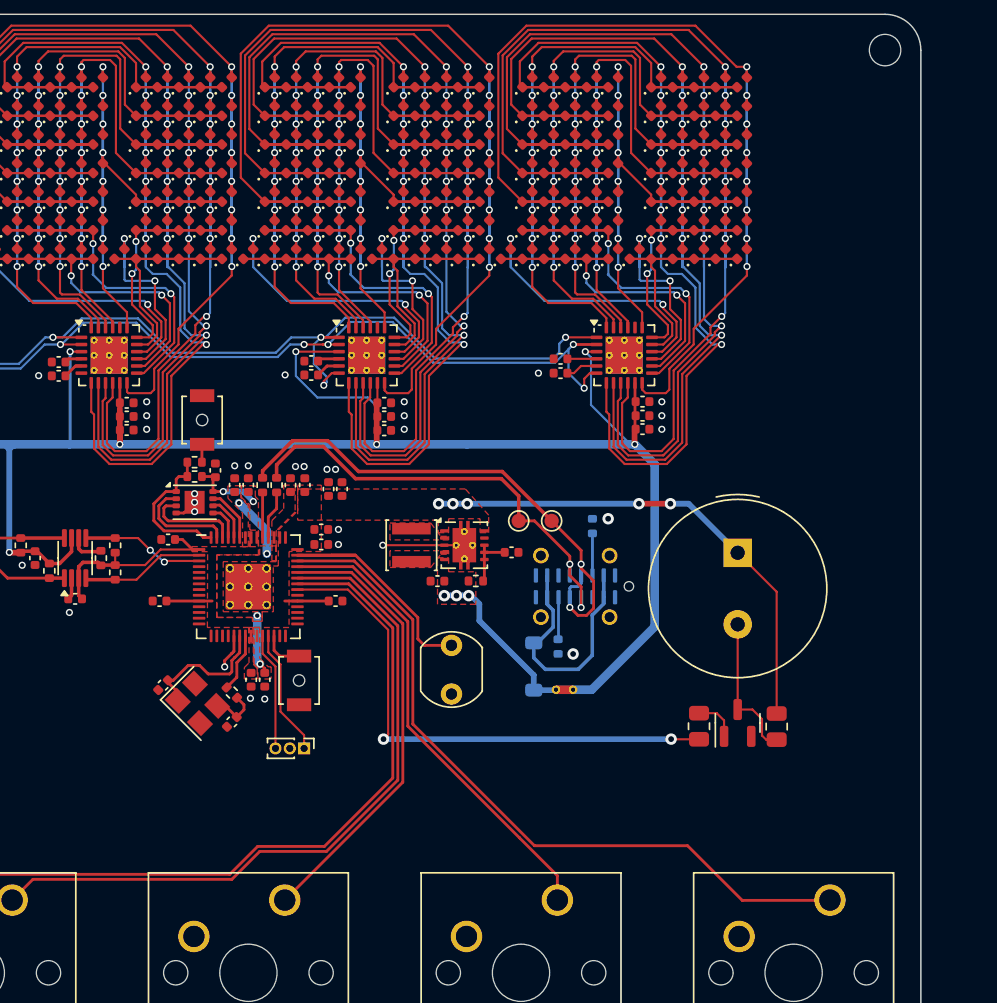
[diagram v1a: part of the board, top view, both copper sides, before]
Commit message: added some silkscreen labels
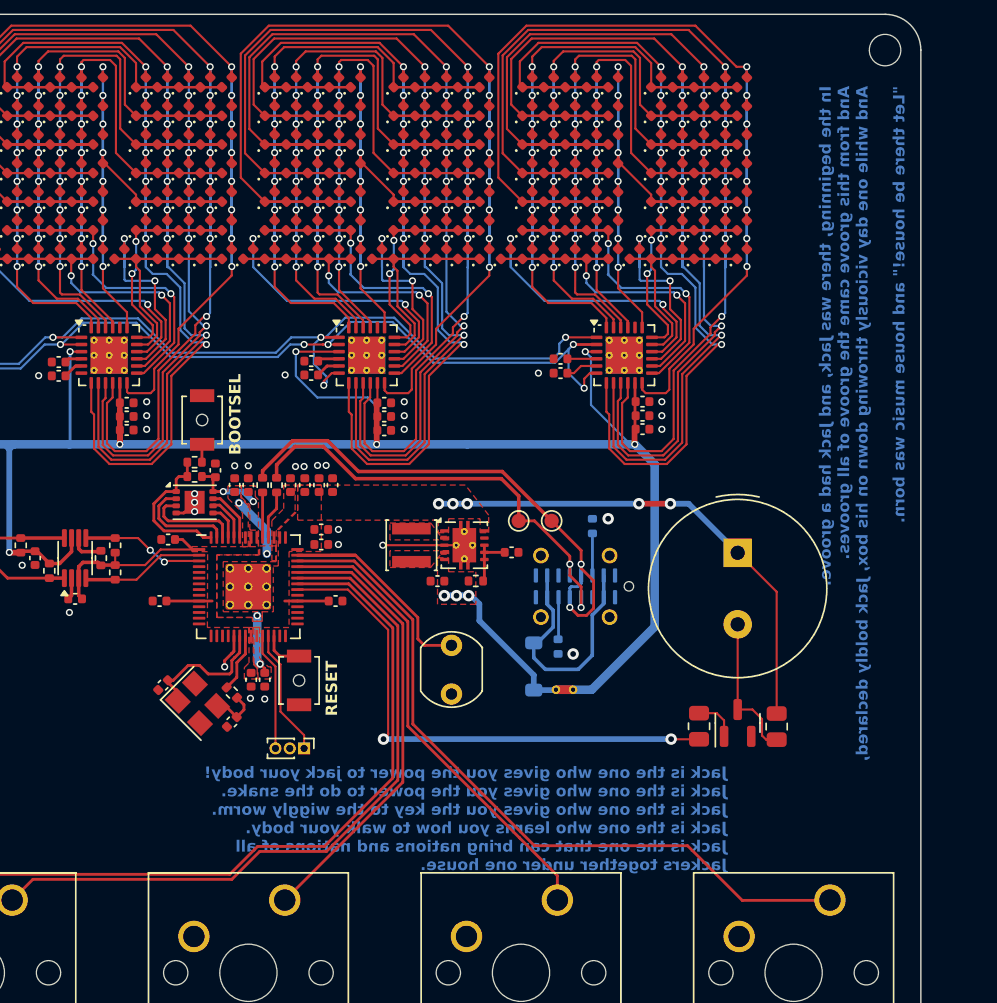
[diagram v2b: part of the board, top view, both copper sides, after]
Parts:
- moved C206 0.72 mm to (73.5, 55.9)
- moved C207 0.72 mm to (74.4, 55.9)
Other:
- board text added: "BOOTSEL"
- board text added: "In the beginning, there was Jack, and Jack had a groove. And from this groove came the groove of all grooves. And while one day viciously throwing down on his box, Jack boldly declared, {dblquote}Let there be house!{dblquote} and house music was born."
- board text added: "Jack is the one who gives you the power to jack your body! Jack is the one who gives you the power to do the snake. Jack is the one who gives you the key to the wiggly worm. Jack is the one who learns you how to walk your body. Jack is the one that can bring nations and nations of all Jackers together under one house."
- board text added: "RESET"

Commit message: small corrections
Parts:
- R201, R202: value 5.1K 0402 -> 5K1 0402
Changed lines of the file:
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@@
 		(property ki_fp_filters "C_*")
 		(sheetname "Onboard Pico")
-		(sheetfile "untitled.kicad_sch")
+		(sheetfile "MCU.kicad_sch")
 		(attr smd)
 		(fp_line
@@
 		(property ki_fp_filters "R_*")
 		(sheetname "Onboard Pico")
-		(sheetfile "untitled.kicad_sch")
+		(sheetfile "MCU.kicad_sch")
 		(attr smd)
 		(fp_line
@@
 		(property ki_fp_filters "R_*")
 		(sheetname "Onboard Pico")
-		(sheetfile "untitled.kicad_sch")
+		(sheetfile "MCU.kicad_sch")
 		(attr smd)
 		(fp_line
@@
 		(property ki_fp_filters "C_*")
 		(sheetname "Onboard Pico")
-		(sheetfile "untitled.kicad_sch")
+		(sheetfile "MCU.kicad_sch")
 		(attr smd)
 		(fp_line
@@
 		(property ki_fp_filters "R_*")
 		(sheetname "Onboard Pico")
-		(sheetfile "untitled.kicad_sch")
+		(sheetfile "MCU.kicad_sch")
 		(attr smd)
 		(fp_line
@@
 		(property ki_fp_filters "C_*")
 		(sheetname "Onboard Pico")
-		(sheetfile "untitled.kicad_sch")
+		(sheetfile "MCU.kicad_sch")
 		(attr smd)
 		(fp_line
@@
 		(property ki_fp_filters "R_*")
 		(sheetname "Onboard Pico")
-		(sheetfile "untitled.kicad_sch")
+		(sheetfile "MCU.kicad_sch")
 		(attr smd)
 		(fp_line
@@
 		)
 		(sheetname "Onboard Pico")
-		(sheetfile "untitled.kicad_sch")
+		(sheetfile "MCU.kicad_sch")
 		(attr smd)
 		(fp_line
@@
 		(property ki_fp_filters "C_*")
 		(sheetname "Onboard Pico")
-		(sheetfile "untitled.kicad_sch")
+		(sheetfile "MCU.kicad_sch")
 		(attr smd)
 		(fp_line
@@
 		(property ki_fp_filters "C_*")
 		(sheetname "Onboard Pico")
-		(sheetfile "untitled.kicad_sch")
+		(sheetfile "MCU.kicad_sch")
 		(attr smd)
 		(fp_line
@@
 		(property ki_fp_filters "C_*")
 		(sheetname "Onboard Pico")
-		(sheetfile "untitled.kicad_sch")
+		(sheetfile "MCU.kicad_sch")
 		(attr smd)
 		(fp_line
@@
 		(property ki_fp_filters "Pin* Test*")
 		(sheetname "Onboard Pico")
-		(sheetfile "untitled.kicad_sch")
+		(sheetfile "MCU.kicad_sch")
 		(attr exclude_from_pos_files)
 		(fp_circle
@@
 		(property ki_fp_filters "Pin* Test*")
 		(sheetname "Onboard Pico")
-		(sheetfile "untitled.kicad_sch")
+		(sheetfile "MCU.kicad_sch")
 		(attr exclude_from_pos_files)
 		(fp_circle
@@
 		(property ki_fp_filters "Crystal*")
 		(sheetname "Onboard Pico")
-		(sheetfile "untitled.kicad_sch")
+		(sheetfile "MCU.kicad_sch")
 		(attr smd)
 		(fp_line
@@
 		(property ki_fp_filters "C_*")
 		(sheetname "Onboard Pico")
-		(sheetfile "untitled.kicad_sch")
+		(sheetfile "MCU.kicad_sch")
 		(attr smd)
 		(fp_line
@@
 		(property ki_fp_filters "Texas*DRC0010J*")
 		(sheetname "Onboard Pico")
-		(sheetfile "untitled.kicad_sch")
+		(sheetfile "MCU.kicad_sch")
 		(attr smd)
 		(fp_line
@@
 		(property ki_fp_filters "C_*")
 		(sheetname "Onboard Pico")
-		(sheetfile "untitled.kicad_sch")
+		(sheetfile "MCU.kicad_sch")
 		(attr smd)
 		(fp_line
@@
 		)
 		(sheetname "Onboard Pico")
-		(sheetfile "untitled.kicad_sch")
+		(sheetfile "MCU.kicad_sch")
 		(attr smd)
 		(fp_line
@@
 		(property ki_fp_filters "C_*")
 		(sheetname "Onboard Pico")
-		(sheetfile "untitled.kicad_sch")
+		(sheetfile "MCU.kicad_sch")
 		(attr smd)
 		(fp_line
@@
 		(property ki_fp_filters "Choke_* *Coil* Inductor_* L_*")
 		(sheetname "Onboard Pico")
-		(sheetfile "untitled.kicad_sch")
+		(sheetfile "MCU.kicad_sch")
 		(attr smd)
 		(fp_line
@@
 		(property ki_fp_filters "C_*")
 		(sheetname "Onboard Pico")
-		(sheetfile "untitled.kicad_sch")
+		(sheetfile "MCU.kicad_sch")
 		(attr smd)
 		(fp_line
@@
 		(property ki_fp_filters "C_*")
 		(sheetname "Onboard Pico")
-		(sheetfile "untitled.kicad_sch")
+		(sheetfile "MCU.kicad_sch")
 		(attr smd)
 		(fp_line
@@
 		(property ki_fp_filters "C_*")
 		(sheetname "Onboard Pico")
-		(sheetfile "untitled.kicad_sch")
+		(sheetfile "MCU.kicad_sch")
 		(attr smd)
 		(fp_line
@@
 		(property ki_fp_filters "C_*")
 		(sheetname "Onboard Pico")
-		(sheetfile "untitled.kicad_sch")
+		(sheetfile "MCU.kicad_sch")
 		(attr smd)
 		(fp_line
@@
 		(property ki_fp_filters "R_*")
 		(sheetname "Onboard Pico")
-		(sheetfile "untitled.kicad_sch")
+		(sheetfile "MCU.kicad_sch")
 		(attr smd)
 		(fp_line
@@
 		(property ki_fp_filters "C_*")
 		(sheetname "Onboard Pico")
-		(sheetfile "untitled.kicad_sch")
+		(sheetfile "MCU.kicad_sch")
 		(attr smd)
 		(fp_line
@@
 		(property ki_fp_filters "R_*")
 		(sheetname "Onboard Pico")
-		(sheetfile "untitled.kicad_sch")
+		(sheetfile "MCU.kicad_sch")
 		(attr smd)
 		(fp_line
@@
 		(property ki_fp_filters "C_*")
 		(sheetname "Onboard Pico")
-		(sheetfile "untitled.kicad_sch")
+		(sheetfile "MCU.kicad_sch")
 		(attr smd)
 		(fp_line
@@
 		(property ki_fp_filters "WSON*1EP*6x5mm*P1.27mm*")
 		(sheetname "Onboard Pico")
-		(sheetfile "untitled.kicad_sch")
+		(sheetfile "MCU.kicad_sch")
 		(attr smd)
 		(fp_line
@@
 		(property ki_fp_filters "C_*")
 		(sheetname "Onboard Pico")
-		(sheetfile "untitled.kicad_sch")
+		(sheetfile "MCU.kicad_sch")
 		(attr smd)
 		(fp_line
@@
 		(property ki_fp_filters "C_*")
 		(sheetname "Onboard Pico")
-		(sheetfile "untitled.kicad_sch")
+		(sheetfile "MCU.kicad_sch")
 		(attr smd)
 		(fp_line
@@
 		)
 		(sheetname "Onboard Pico")
-		(sheetfile "untitled.kicad_sch")
+		(sheetfile "MCU.kicad_sch")
 		(attr smd)
 		(fp_line
@@
 		(property ki_fp_filters "C_*")
 		(sheetname "Onboard Pico")
-		(sheetfile "untitled.kicad_sch")
+		(sheetfile "MCU.kicad_sch")
 		(attr smd)
 		(fp_line
@@
 			)
 		)
-		(property "Value" "5.1K 0402"
+		(property "Value" "5K1 0402"
 			(at 0 -1.17 90)
 			(layer "B.Fab")
@@
 		(property ki_fp_filters "R_*")
 		(sheetname "Onboard Pico")
-		(sheetfile "untitled.kicad_sch")
+		(sheetfile "MCU.kicad_sch")
 		(attr smd)
 		(fp_line
@@
 		(property ki_fp_filters "USB*C*Receptacle*")
 		(sheetname "Onboard Pico")
-		(sheetfile "untitled.kicad_sch")
+		(sheetfile "MCU.kicad_sch")
 		(attr smd)
 		(fp_line
@@
 		(property ki_fp_filters "TO-???* *_Diode_* *SingleDiode* D_*")
 		(sheetname "Onboard Pico")
-		(sheetfile "untitled.kicad_sch")
+		(sheetfile "MCU.kicad_sch")
 		(attr smd)
 		(fp_line
@@
 			)
 		)
-		(property "Value" "5.1K 0402"
+		(property "Value" "5K1 0402"
 			(at 0 -1.17 90)
 			(layer "B.Fab")
@@
 		(property ki_fp_filters "R_*")
 		(sheetname "Onboard Pico")
-		(sheetfile "untitled.kicad_sch")
+		(sheetfile "MCU.kicad_sch")
 		(attr smd)
 		(fp_line
@@
 		(polygon
 			(pts
-				(xy 71.775 55.9) (xy 71.775 57.775) (xy 70.476385 59.073615) (xy 70.448839 59.073615) (xy 70.448839 60.148839)
-				(xy 70.448839 61.178615) (xy 70.150224 61.18) (xy 70.148839 60.148615) (xy 70.148839 58.376161)
-				(xy 70.975 57.55) (xy 70.975 55.9)
+				(xy 71.775 55.9) (xy 71.775 57.6) (xy 70.448839 58.873615) (xy 70.448839 60.148839) (xy 70.448839 61.178615)
+				(xy 70.150224 61.18) (xy 70.148839 60.148615) (xy 70.148839 58.376161) (xy 70.975 57.55) (xy 70.975 55.9)
 			)
 		)
